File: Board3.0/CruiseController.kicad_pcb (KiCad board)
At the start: 2 copper layers, 23.1 x 38 mm, 55 parts, among them J1 USB_B_Micro, J2 Conn_02x09_Top_Bottom, U1 ADG884, U3 TLV9064IRTER, U5 MIC5225, U6 MCP2562-E-MF, U7 STM32L433CCUx, Y1 32.768

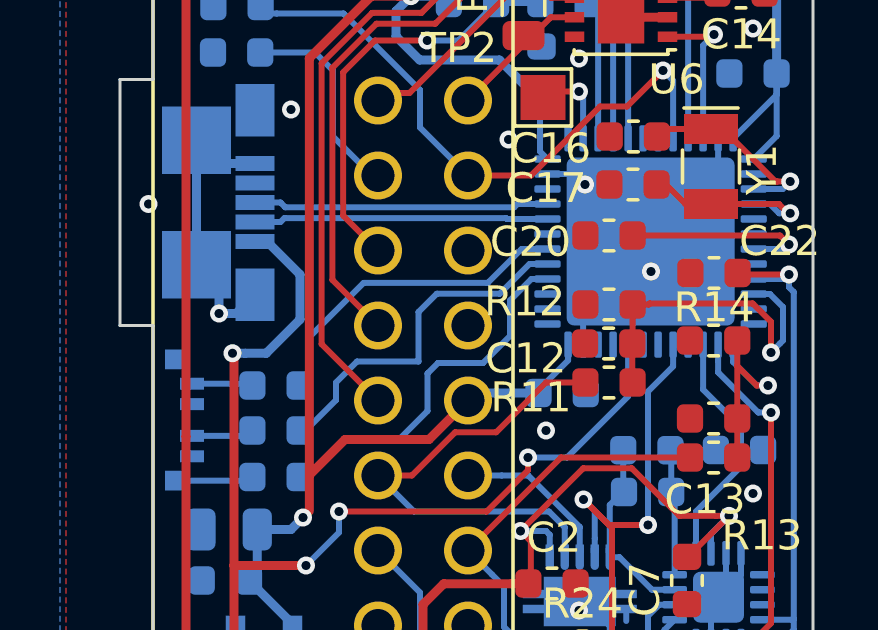
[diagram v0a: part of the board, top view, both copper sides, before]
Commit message: fix LED PWM pins
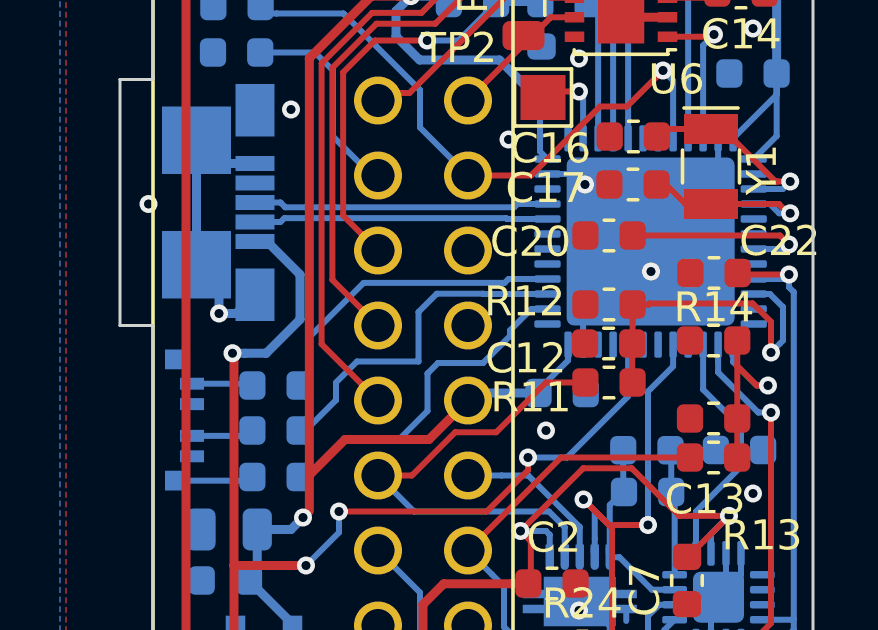
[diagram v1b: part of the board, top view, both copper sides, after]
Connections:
- J1 pad 4: Net-(J1-Pad4) -> (no net)
- U3 pad 5: Net-(U3-Pad5) -> (no net)
- U5 pad 4: Net-(U5-Pad4) -> (no net)
- U7 pad 11: Net-(U7-Pad11) -> (no net)
- U7 pad 12: Net-(U7-Pad12) -> (no net)
- U7 pad 16: Net-(U7-Pad16) -> (no net)
- U7 pad 18: Net-(U7-Pad18) -> (no net)
- U7 pad 19: Net-(U7-Pad19) -> (no net)
- U7 pad 2: Net-(U7-Pad2) -> (no net)
- U7 pad 21: Net-(U7-Pad21) -> (no net)
- U7 pad 22: Net-(U7-Pad22) -> (no net)
- U7 pad 25: Net-(U7-Pad25) -> (no net)
- U7 pad 26: Net-(U7-Pad26) -> LEDB
- U7 pad 27: Net-(U7-Pad27) -> LEDR
- U7 pad 28: LEDB -> LEDG
- U7 pad 29: LEDR -> (no net)
- U7 pad 30: LEDG -> (no net)
- U7 pad 31: Net-(U7-Pad31) -> (no net)
- U7 pad 34: Net-(U7-Pad34) -> (no net)
- U7 pad 37: Net-(U7-Pad37) -> (no net)
- U7 pad 42: Net-(U7-Pad42) -> (no net)
- U7 pad 43: Net-(U7-Pad43) -> (no net)
- U7 pad 5: Net-(U7-Pad5) -> (no net)
- U7 pad 6: Net-(U7-Pad6) -> (no net)
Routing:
- net LEDB: track 12.0 -> 11.0 mm

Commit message: Update v3
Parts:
- D2, F1: moved to B.Cu
- R1: value 10k -> 2.2k
- moved D2 5.84 mm to (109.7, 101.5), turned to 180 degrees
- moved F1 3.31 mm to (115.2, 103.8), turned to 180 degrees
- moved C6 0.25 mm to (104.1, 100.8)
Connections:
- J1 pad 4: (no net) -> Net-(J1-Pad4)
- U3 pad 4: GND -> Net-(U3-Pad4)
- U3 pad 5: (no net) -> Net-(U3-Pad4)
- U5 pad 4: (no net) -> Net-(U5-Pad4)
- U7 pad 11: (no net) -> Net-(U7-Pad11)
- U7 pad 12: (no net) -> Net-(U7-Pad12)
- U7 pad 16: (no net) -> Net-(U7-Pad16)
- U7 pad 18: (no net) -> Net-(U7-Pad18)
- U7 pad 19: (no net) -> Net-(U7-Pad19)
- U7 pad 2: (no net) -> Net-(U7-Pad2)
- U7 pad 21: (no net) -> Net-(U7-Pad21)
- U7 pad 22: (no net) -> Net-(U7-Pad22)
- U7 pad 25: (no net) -> Net-(U7-Pad25)
- U7 pad 29: (no net) -> Net-(U7-Pad29)
- U7 pad 30: (no net) -> Net-(U7-Pad30)
- U7 pad 31: (no net) -> Net-(U7-Pad31)
- U7 pad 34: (no net) -> Net-(U7-Pad34)
- U7 pad 37: (no net) -> Net-(U7-Pad37)
- U7 pad 42: (no net) -> Net-(U7-Pad42)
- U7 pad 43: (no net) -> Net-(U7-Pad43)
- U7 pad 5: (no net) -> Net-(U7-Pad5)
- U7 pad 6: (no net) -> Net-(U7-Pad6)
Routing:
- net GND: track 40.9 -> 39.1 mm
- net VUSB: track 56.5 -> 55.1 mm, vias 4 -> 5
- net Net-(U3-Pad4): track 0.00 -> 1.24 mm
- net REGIN: track 115.5 -> 115.2 mm, vias 5 -> 4

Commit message: Update V3
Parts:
- removed C17: 8pF, Capacitor_SMD:C_0603_1608Metric
- added C11: 8pF, Capacitor_SMD:C_0603_1608Metric, F.Cu at (116.8, 81.7)
- added C8: 4.7uF, Capacitor_SMD:C_0805_2012Metric, B.Cu at (119.7, 72.3)
- added R22: 50, Resistor_SMD:R_0603_1608Metric, B.Cu at (105.6, 88.0)
- R10, R9: value 27 -> 50
- R21: value 85 -> 50
- R24, TP2: moved to B.Cu
- moved TP2 12.1 mm to (113.3, 91.0)
- moved R4 9.65 mm to (110.1, 105.2), turned to 180 degrees
- moved C20 7.82 mm to (121.1, 78.3), turned to 90 degrees
- moved R13 5.93 mm to (112.8, 91.6), turned to 270 degrees
- moved R14 5.53 mm to (115.6, 91.6), turned to 90 degrees
- moved R24 5.31 mm to (113.8, 102.5), turned to 90 degrees
- moved C13 4.91 mm to (114.2, 91.6), turned to 270 degrees
- moved C5 4.81 mm to (116.4, 104.3), turned to 180 degrees
- moved C3 4.61 mm to (120.3, 103.6), turned to 0 degrees
- moved F1 4.53 mm to (110.7, 103.3), turned to 0 degrees
- moved R10 3.53 mm to (105.1, 85.1), turned to 270 degrees
- moved C16 3.49 mm to (116.8, 83.6), turned to 180 degrees
- moved R7 3.18 mm to (116.4, 102.9)
- moved C2 2.74 mm to (114.4, 97.6)
- moved C7 2.47 mm to (118.7, 97.3)
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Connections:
- C16 pad 1: GND -> Net-(C16-Pad1)
- C16 pad 2: Net-(C16-Pad2) -> GND
- R21 pad 1: LEDR -> Net-(R21-Pad1)
- U7 pad 18: Net-(U7-Pad18) -> Net-(TP2-Pad1)
- U7 pad 20: VUSB -> Net-(U7-Pad20)
- U7 pad 3: Net-(C16-Pad2) -> Net-(C11-Pad1)
- U7 pad 38: Net-(TP2-Pad1) -> Net-(U7-Pad38)
- U7 pad 39: BUTTONUP -> Net-(U7-Pad39)
- U7 pad 4: Net-(C17-Pad2) -> Net-(C16-Pad1)
- U7 pad 40: BUTTONMID -> BUTTONUP
- U7 pad 41: BUTTONDOWN -> BUTTONMID
- U7 pad 42: Net-(U7-Pad42) -> BUTTONDOWN
- Y1 pad 1: Net-(C16-Pad2) -> Net-(C16-Pad1)
- Y1 pad 2: Net-(C17-Pad2) -> Net-(C11-Pad1)
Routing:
- net VUSB: track 55.1 -> 26.6 mm, vias 5 -> 2
- net REGIN: track 115.2 -> 95.2 mm, vias 4 -> 3
- net BOOT0: track 20.2 -> 35.8 mm, vias 1 -> 2
- net Net-(C3-Pad1): track 5.27 -> 13.9 mm
- net Net-(C16-Pad2): track 6.59 -> 0.00 mm, vias 1 -> 0
- net Net-(C17-Pad2): track 6.19 -> 0.00 mm, vias 1 -> 0
- net Net-(C16-Pad1): track 0.00 -> 5.30 mm, vias 0 -> 1
- net Net-(C11-Pad1): track 0.00 -> 5.04 mm, vias 0 -> 1
- net VREFB: track 6.96 -> 10.6 mm
- net TTBIN: track 13.5 -> 9.93 mm
- net Net-(D1-Pad5): track 2.24 -> 5.09 mm
- net Net-(TP2-Pad1): track 2.90 -> 5.57 mm, vias 1 -> 0
- net Net-(C5-Pad2): track 9.53 -> 11.8 mm
- net VIN: track 10.6 -> 8.58 mm
- net VREFA: track 11.3 -> 9.56 mm
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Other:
- board size 23.1 x 38 mm -> 24 x 38 mm
